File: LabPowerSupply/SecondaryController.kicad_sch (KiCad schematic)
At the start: 18 parts, among them Y2 8M

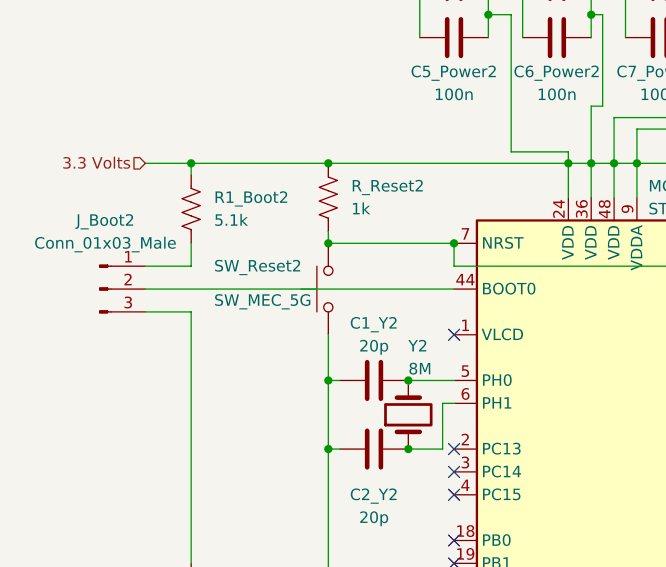
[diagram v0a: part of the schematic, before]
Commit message: Figured out how to make fill zones
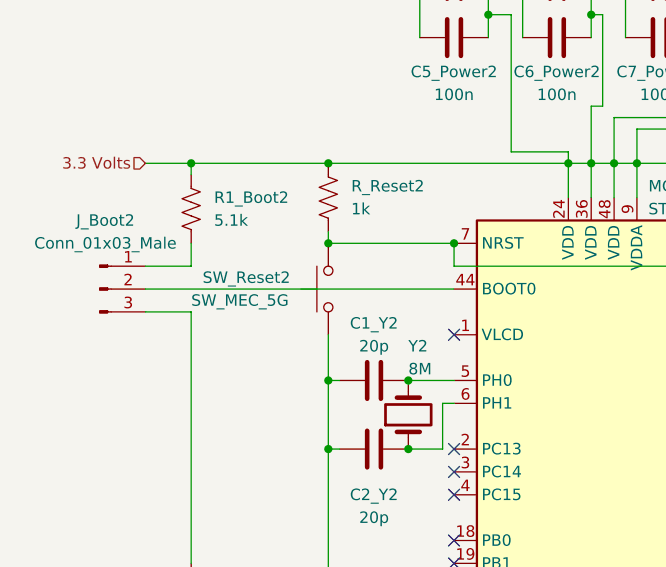
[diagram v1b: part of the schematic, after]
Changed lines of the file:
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@@
   (junction (at 116.84 139.7) (diameter 0) (color 0 0 0 0)
   )
+  (junction (at 68.58 63.5) (diameter 0) (color 0 0 0 0)
+  )
   (junction (at 68.58 54.61) (diameter 0) (color 0 0 0 0)
   )
@@
   (junction (at 101.6 30.48) (diameter 0) (color 0 0 0 0)
   )
-  (junction (at 68.58 63.5) (diameter 0) (color 0 0 0 0)
+  (junction (at 82.55 63.5) (diameter 0) (color 0 0 0 0)
   )
   (junction (at 68.58 139.7) (diameter 0) (color 0 0 0 0)
@@
   )
   (junction (at 86.36 38.1) (diameter 0) (color 0 0 0 0)
-  )
-  (junction (at 82.55 63.5) (diameter 0) (color 0 0 0 0)
   )
   (junction (at 77.47 78.74) (diameter 0) (color 0 0 0 0)
@@
     (stroke (width 0) (type default) (color 0 0 0 0))
   )
+  (wire (pts (xy 100.33 54.61) (xy 102.87 54.61))
+    (stroke (width 0) (type default) (color 0 0 0 0))
+  )
+  (wire (pts (xy 106.68 138.43) (xy 106.68 66.04))
+    (stroke (width 0) (type default) (color 0 0 0 0))
+  )
+  (wire (pts (xy 48.26 66.04) (xy 53.34 66.04))
+    (stroke (width 0) (type default) (color 0 0 0 0))
+  )
+  (wire (pts (xy 102.87 50.8) (xy 102.87 54.61))
+    (stroke (width 0) (type default) (color 0 0 0 0))
+  )
   (wire (pts (xy 68.58 63.5) (xy 82.55 63.5))
-    (stroke (width 0) (type default) (color 0 0 0 0))
-  )
-  (wire (pts (xy 100.33 54.61) (xy 102.87 54.61))
-    (stroke (width 0) (type default) (color 0 0 0 0))
-  )
-  (wire (pts (xy 106.68 138.43) (xy 106.68 66.04))
-    (stroke (width 0) (type default) (color 0 0 0 0))
-  )
-  (wire (pts (xy 48.26 66.04) (xy 53.34 66.04))
-    (stroke (width 0) (type default) (color 0 0 0 0))
-  )
-  (wire (pts (xy 102.87 50.8) (xy 102.87 54.61))
     (stroke (width 0) (type default) (color 0 0 0 0))
   )
@@
     (pin "2")
   )
+  (symbol (lib_id "Switch:SW_MEC_5G") (at 68.58 68.58 90) (unit 1)
+    (in_bom yes) (on_board yes)
+    (property "Reference" "SW_Reset2" (id 0) (at 54.61 67.31 90)
+      (effects (font (size 1.27 1.27)) (justify right))
+    )
+    (property "Value" "SW_MEC_5G" (id 1) (at 53.34 69.85 90)
+      (effects (font (size 1.27 1.27)) (justify right))
+    )
+    (property "Footprint" "Button_Switch_THT:SW_PUSH-12mm" (id 2) (at 63.5 68.58 0)
+      (effects (font (size 1.27 1.27)) hide)
+    )
+    (property "Datasheet" "http://www.apem.com/int/index.php?controller=attachment&id_attachment=488" (id 3) (at 63.5 68.58 0)
+      (effects (font (size 1.27 1.27)) hide)
+    )
+    (pin "1")
+    (pin "3")
+    (pin "2")
+    (pin "4")
+  )
   (symbol (lib_id "Device:C") (at 105.41 34.29 90) (unit 1)
     (in_bom yes) (on_board yes) (fields_autoplaced)
@@
     (pin "2")
   )
-  (symbol (lib_id "Switch:SW_MEC_5G") (at 68.58 68.58 90) (unit 1)
-    (in_bom yes) (on_board yes)
-    (property "Reference" "SW_Reset2" (id 0) (at 55.88 66.04 90)
-      (effects (font (size 1.27 1.27)) (justify right))
-    )
-    (property "Value" "SW_MEC_5G" (id 1) (at 55.88 69.85 90)
-      (effects (font (size 1.27 1.27)) (justify right))
-    )
-    (property "Footprint" "Button_Switch_THT:SW_PUSH-12mm" (id 2) (at 63.5 68.58 0)
-      (effects (font (size 1.27 1.27)) hide)
-    )
-    (property "Datasheet" "http://www.apem.com/int/index.php?controller=attachment&id_attachment=488" (id 3) (at 63.5 68.58 0)
-      (effects (font (size 1.27 1.27)) hide)
-    )
-    (pin "1")
-    (pin "3")
-    (pin "2")
-    (pin "4")
-  )
 )

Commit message: Traces
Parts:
- SW_Reset2: symbol Switch:SW_MEC_5G -> Switch:SW_Push
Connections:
- net GND: no longer SW_Reset2.2 (A)
- net at J_STLink2.5 (Pin_5), MCU_2.7 (NRST), R_Reset2.2: now also SW_Reset2.2; no longer SW_Reset2.3 (B), SW_Reset2.4 (B)
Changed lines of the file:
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@@
     (pin "2")
   )
-  (symbol (lib_id "Switch:SW_MEC_5G") (at 68.58 68.58 90) (unit 1)
+  (symbol (lib_id "Switch:SW_Push") (at 68.58 68.58 90) (unit 1)
     (in_bom yes) (on_board yes)
     (property "Reference" "SW_Reset2" (id 0) (at 54.61 67.31 90)
@@
       (effects (font (size 1.27 1.27)) hide)
     )
-    (property "Datasheet" "http://www.apem.com/int/index.php?controller=attachment&id_attachment=488" (id 3) (at 63.5 68.58 0)
+    (property "Datasheet" "~" (id 3) (at 63.5 68.58 0)
       (effects (font (size 1.27 1.27)) hide)
     )
     (pin "1")
-    (pin "3")
     (pin "2")
-    (pin "4")
   )
   (symbol (lib_id "Device:C") (at 105.41 34.29 90) (unit 1)

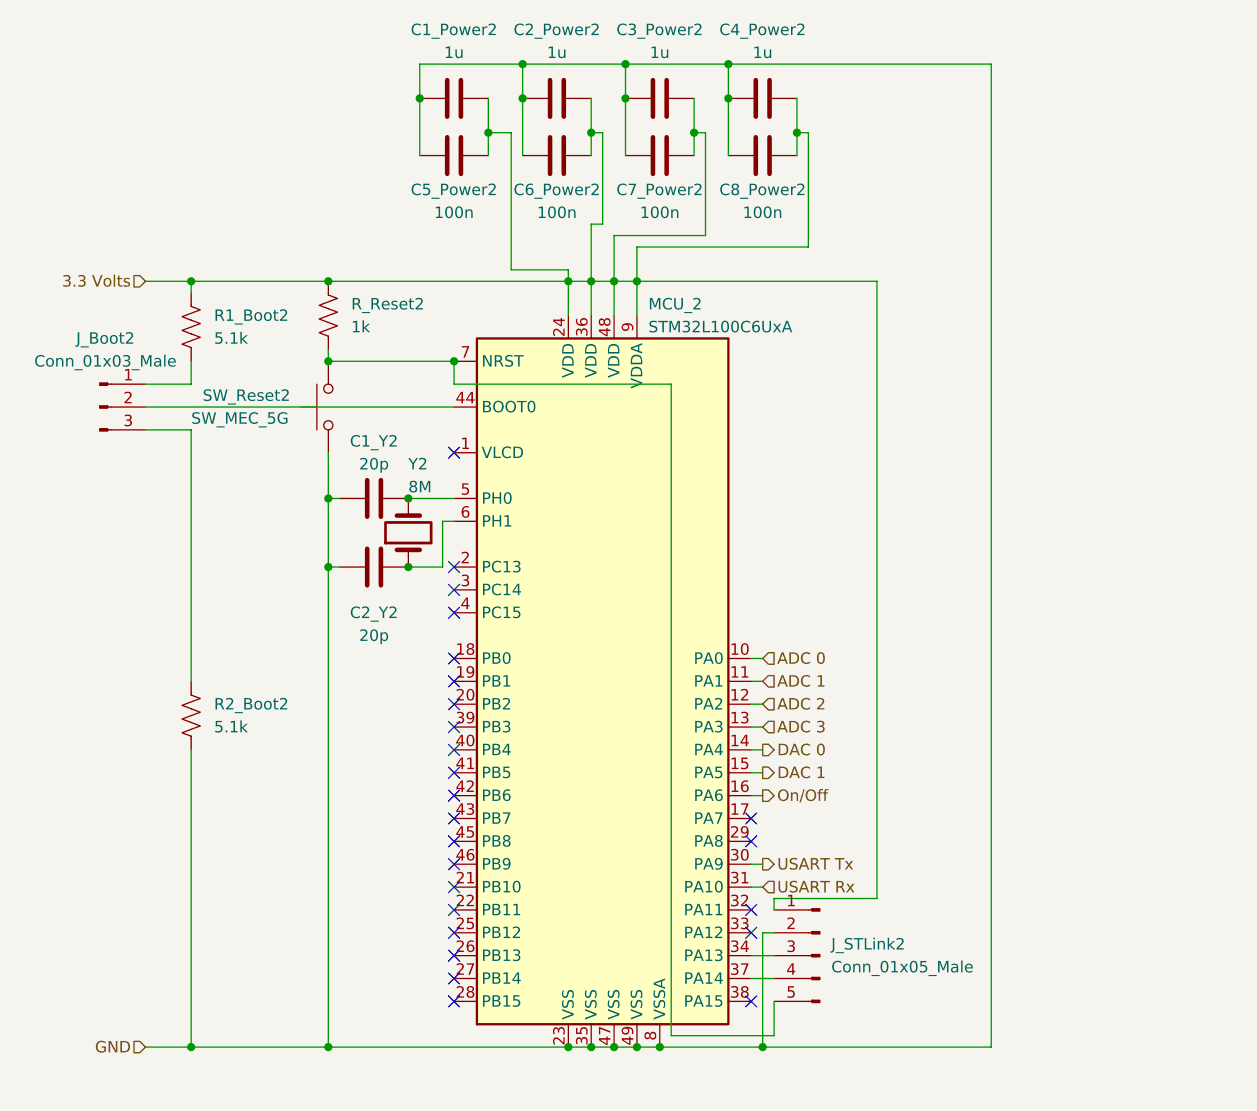
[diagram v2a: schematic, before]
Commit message: Started ch2 MCU routing
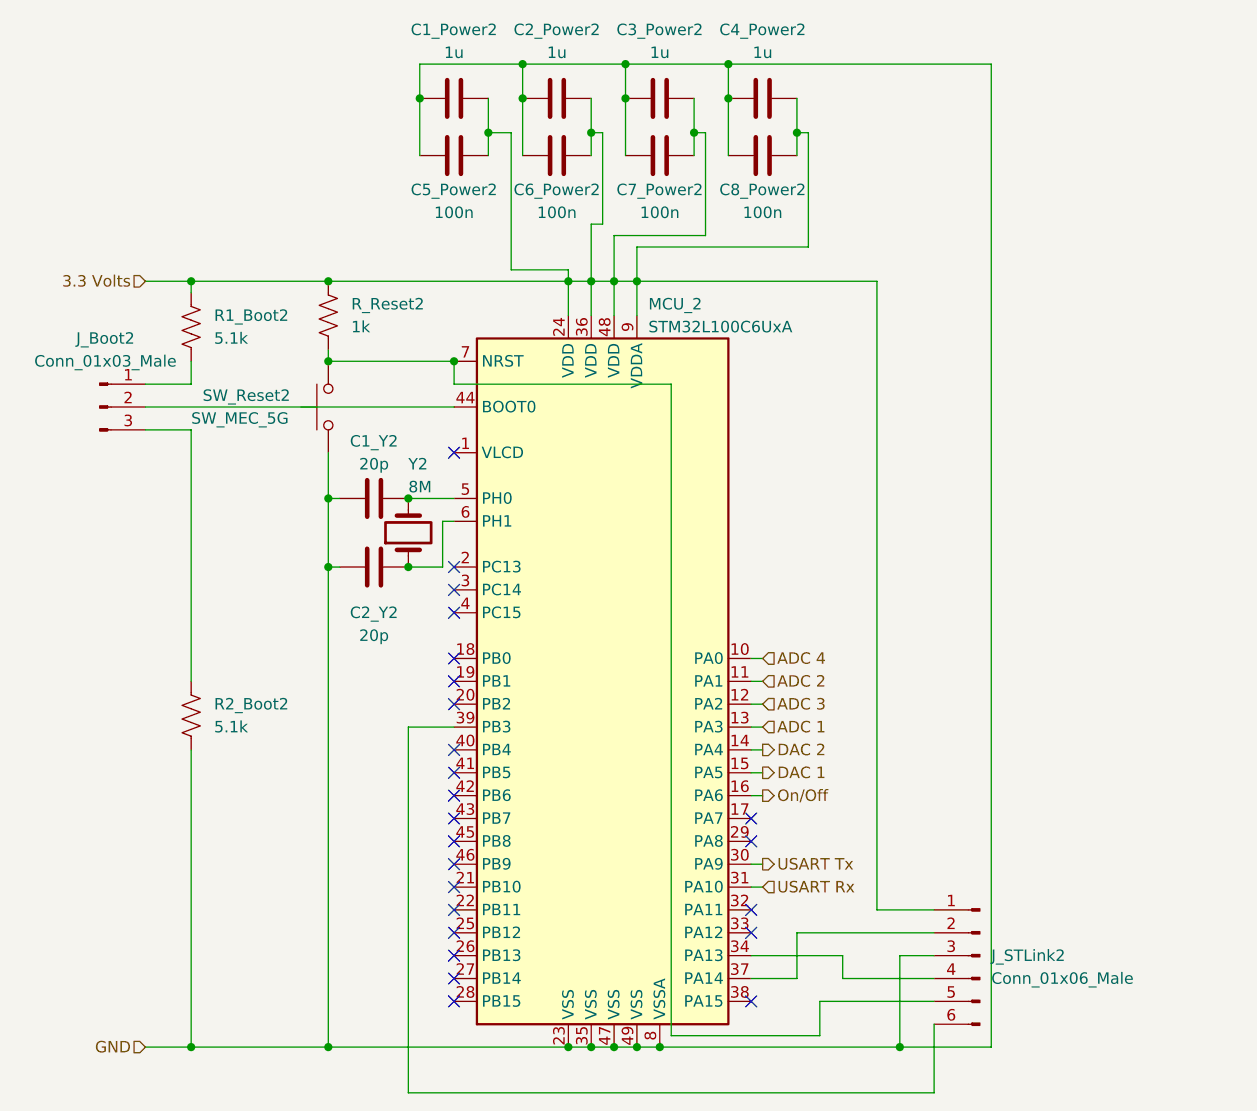
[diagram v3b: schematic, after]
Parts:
- removed J_STLink2: Conn_01x05_Male, Connector_PinHeader_2.54mm:PinHeader_1x05_P2.54mm_Vertical, symbol Connector:Conn_01x05_Male
- added J_STLink2: Conn_01x06_Male, Connector_PinHeader_2.54mm:PinHeader_1x06_P2.54mm_Vertical, symbol Connector:Conn_01x06_Male
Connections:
- net 3.3 Volts: now also J_STLink2.1 (Pin_1)
- net ADC 1: now also MCU_2.13 (PA3); no longer MCU_2.11 (PA1)
- net ADC 2: now also MCU_2.11 (PA1); no longer MCU_2.12 (PA2)
- net ADC 3: now also MCU_2.12 (PA2); no longer MCU_2.13 (PA3)
- net GND: now also J_STLink2.3 (Pin_3)
- net at MCU_2.34 (PA13): now also J_STLink2.4 (Pin_4)
- net at MCU_2.37 (PA14): now also J_STLink2.2 (Pin_2)
- net at MCU_2.7 (NRST), R_Reset2.2, SW_Reset2.2: now also J_STLink2.5 (Pin_5)
- net at MCU_2.39 (PB3): now also J_STLink2.6 (Pin_6)
- net ADC 0 renamed ADC 4
- net DAC 0 renamed DAC 2
- no-connect marks 25 -> 24
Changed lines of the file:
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@@
   (junction (at 102.87 139.7) (diameter 0) (color 0 0 0 0)
   )
-  (junction (at 116.84 139.7) (diameter 0) (color 0 0 0 0)
-  )
   (junction (at 68.58 63.5) (diameter 0) (color 0 0 0 0)
   )
@@
   )
   (junction (at 97.79 139.7) (diameter 0) (color 0 0 0 0)
+  )
+  (junction (at 132.08 139.7) (diameter 0) (color 0 0 0 0)
   )
   (junction (at 109.22 38.1) (diameter 0) (color 0 0 0 0)
@@
   (no_connect (at 82.55 109.22))
   (no_connect (at 82.55 106.68))
-  (no_connect (at 82.55 104.14))
   (no_connect (at 82.55 121.92))
   (no_connect (at 82.55 119.38))
@@
     (stroke (width 0) (type default) (color 0 0 0 0))
   )
+  (wire (pts (xy 82.55 104.14) (xy 77.47 104.14))
+    (stroke (width 0) (type default) (color 0 0 0 0))
+  )
   (wire (pts (xy 48.26 71.12) (xy 53.34 71.12))
     (stroke (width 0) (type default) (color 0 0 0 0))
@@
     (stroke (width 0) (type default) (color 0 0 0 0))
   )
-  (wire (pts (xy 118.11 123.19) (xy 129.54 123.19))
-    (stroke (width 0) (type default) (color 0 0 0 0))
-  )
   (wire (pts (xy 97.79 34.29) (xy 97.79 38.1))
     (stroke (width 0) (type default) (color 0 0 0 0))
   )
+  (wire (pts (xy 120.65 127) (xy 135.89 127))
+    (stroke (width 0) (type default) (color 0 0 0 0))
+  )
   (wire (pts (xy 86.36 38.1) (xy 88.9 38.1))
     (stroke (width 0) (type default) (color 0 0 0 0))
   )
+  (wire (pts (xy 129.54 124.46) (xy 135.89 124.46))
+    (stroke (width 0) (type default) (color 0 0 0 0))
+  )
   (wire (pts (xy 100.33 54.61) (xy 102.87 54.61))
     (stroke (width 0) (type default) (color 0 0 0 0))
@@
     (stroke (width 0) (type default) (color 0 0 0 0))
   )
-  (wire (pts (xy 118.11 127) (xy 116.84 127))
-    (stroke (width 0) (type default) (color 0 0 0 0))
-  )
   (wire (pts (xy 115.57 121.92) (xy 116.84 121.92))
     (stroke (width 0) (type default) (color 0 0 0 0))
   )
+  (wire (pts (xy 125.73 129.54) (xy 125.73 132.08))
+    (stroke (width 0) (type default) (color 0 0 0 0))
+  )
+  (wire (pts (xy 132.08 139.7) (xy 142.24 139.7))
+    (stroke (width 0) (type default) (color 0 0 0 0))
+  )
+  (wire (pts (xy 77.47 104.14) (xy 77.47 144.78))
+    (stroke (width 0) (type default) (color 0 0 0 0))
+  )
   (wire (pts (xy 88.9 53.34) (xy 95.25 53.34))
     (stroke (width 0) (type default) (color 0 0 0 0))
   )
-  (wire (pts (xy 118.11 124.46) (xy 118.11 123.19))
+  (wire (pts (xy 132.08 129.54) (xy 132.08 139.7))
     (stroke (width 0) (type default) (color 0 0 0 0))
   )
@@
     (stroke (width 0) (type default) (color 0 0 0 0))
   )
-  (wire (pts (xy 115.57 129.54) (xy 118.11 129.54))
+  (wire (pts (xy 115.57 129.54) (xy 125.73 129.54))
     (stroke (width 0) (type default) (color 0 0 0 0))
   )
@@
     (stroke (width 0) (type default) (color 0 0 0 0))
   )
-  (wire (pts (xy 118.11 134.62) (xy 118.11 138.43))
+  (wire (pts (xy 123.19 134.62) (xy 123.19 138.43))
     (stroke (width 0) (type default) (color 0 0 0 0))
   )
@@
     (stroke (width 0) (type default) (color 0 0 0 0))
   )
-  (wire (pts (xy 129.54 123.19) (xy 129.54 54.61))
+  (wire (pts (xy 129.54 54.61) (xy 129.54 124.46))
     (stroke (width 0) (type default) (color 0 0 0 0))
   )
@@
     (stroke (width 0) (type default) (color 0 0 0 0))
   )
+  (wire (pts (xy 77.47 144.78) (xy 135.89 144.78))
+    (stroke (width 0) (type default) (color 0 0 0 0))
+  )
   (wire (pts (xy 97.79 54.61) (xy 97.79 58.42))
     (stroke (width 0) (type default) (color 0 0 0 0))
@@
     (stroke (width 0) (type default) (color 0 0 0 0))
   )
-  (wire (pts (xy 116.84 127) (xy 116.84 139.7))
-    (stroke (width 0) (type default) (color 0 0 0 0))
-  )
   (wire (pts (xy 81.28 86.36) (xy 77.47 86.36))
     (stroke (width 0) (type default) (color 0 0 0 0))
@@
     (stroke (width 0) (type default) (color 0 0 0 0))
   )
-  (wire (pts (xy 115.57 132.08) (xy 118.11 132.08))
+  (wire (pts (xy 115.57 132.08) (xy 120.65 132.08))
     (stroke (width 0) (type default) (color 0 0 0 0))
   )
@@
     (stroke (width 0) (type default) (color 0 0 0 0))
   )
-  (wire (pts (xy 105.41 139.7) (xy 116.84 139.7))
-    (stroke (width 0) (type default) (color 0 0 0 0))
-  )
   (wire (pts (xy 115.57 96.52) (xy 116.84 96.52))
     (stroke (width 0) (type default) (color 0 0 0 0))
@@
     (stroke (width 0) (type default) (color 0 0 0 0))
   )
+  (wire (pts (xy 120.65 132.08) (xy 120.65 127))
+    (stroke (width 0) (type default) (color 0 0 0 0))
+  )
   (wire (pts (xy 100.33 49.53) (xy 100.33 54.61))
     (stroke (width 0) (type default) (color 0 0 0 0))
@@
     (stroke (width 0) (type default) (color 0 0 0 0))
   )
-  (wire (pts (xy 116.84 139.7) (xy 142.24 139.7))
-    (stroke (width 0) (type default) (color 0 0 0 0))
-  )
   (wire (pts (xy 110.49 38.1) (xy 110.49 49.53))
     (stroke (width 0) (type default) (color 0 0 0 0))
@@
     (stroke (width 0) (type default) (color 0 0 0 0))
   )
-  (wire (pts (xy 118.11 138.43) (xy 106.68 138.43))
+  (wire (pts (xy 123.19 138.43) (xy 106.68 138.43))
     (stroke (width 0) (type default) (color 0 0 0 0))
   )
@@
     (stroke (width 0) (type default) (color 0 0 0 0))
   )
+  (wire (pts (xy 105.41 139.7) (xy 132.08 139.7))
+    (stroke (width 0) (type default) (color 0 0 0 0))
+  )
+  (wire (pts (xy 135.89 144.78) (xy 135.89 137.16))
+    (stroke (width 0) (type default) (color 0 0 0 0))
+  )
+  (wire (pts (xy 123.19 134.62) (xy 135.89 134.62))
+    (stroke (width 0) (type default) (color 0 0 0 0))
+  )
   (wire (pts (xy 101.6 34.29) (xy 101.6 40.64))
     (stroke (width 0) (type default) (color 0 0 0 0))
   )
+  (wire (pts (xy 125.73 132.08) (xy 135.89 132.08))
+    (stroke (width 0) (type default) (color 0 0 0 0))
+  )
   (wire (pts (xy 115.57 104.14) (xy 116.84 104.14))
     (stroke (width 0) (type default) (color 0 0 0 0))
@@
     (stroke (width 0) (type default) (color 0 0 0 0))
   )
-  (hierarchical_label "ADC 3" (shape input) (at 116.84 104.14 0)
+  (wire (pts (xy 135.89 129.54) (xy 132.08 129.54))
+    (stroke (width 0) (type default) (color 0 0 0 0))
+  )
+  (hierarchical_label "ADC 1" (shape input) (at 116.84 104.14 0)
     (effects (font (size 1.27 1.27)) (justify left))
   )
@@
     (effects (font (size 1.27 1.27)) (justify left))
   )
-  (hierarchical_label "ADC 0" (shape input) (at 116.84 96.52 0)
-    (effects (font (size 1.27 1.27)) (justify left))
-  )
-  (hierarchical_label "ADC 1" (shape input) (at 116.84 99.06 0)
-    (effects (font (size 1.27 1.27)) (justify left))
-  )
-  (hierarchical_label "ADC 2" (shape input) (at 116.84 101.6 0)
+  (hierarchical_label "ADC 4" (shape input) (at 116.84 96.52 0)
+    (effects (font (size 1.27 1.27)) (justify left))
+  )
+  (hierarchical_label "ADC 2" (shape input) (at 116.84 99.06 0)
+    (effects (font (size 1.27 1.27)) (justify left))
+  )
+  (hierarchical_label "ADC 3" (shape input) (at 116.84 101.6 0)
     (effects (font (size 1.27 1.27)) (justify left))
   )
@@
     (effects (font (size 1.27 1.27)) (justify left))
   )
-  (hierarchical_label "DAC 0" (shape output) (at 116.84 106.68 0)
+  (hierarchical_label "DAC 2" (shape output) (at 116.84 106.68 0)
     (effects (font (size 1.27 1.27)) (justify left))
   )
@@
     (pin "2")
   )
+  (symbol (lib_id "Connector:Conn_01x06_Male") (at 140.97 129.54 0) (mirror y) (unit 1)
+    (in_bom yes) (on_board yes) (fields_autoplaced)
+    (property "Reference" "J_STLink2" (id 0) (at 142.24 129.5399 0)
+      (effects (font (size 1.27 1.27)) (justify right))
+    )
+    (property "Value" "Conn_01x06_Male" (id 1) (at 142.24 132.0799 0)
+      (effects (font (size 1.27 1.27)) (justify right))
+    )
+    (property "Footprint" "Connector_PinHeader_2.54mm:PinHeader_1x06_P2.54mm_Vertical" (id 2) (at 140.97 129.54 0)
+      (effects (font (size 1.27 1.27)) hide)
+    )
+    (property "Datasheet" "~" (id 3) (at 140.97 129.54 0)
+      (effects (font (size 1.27 1.27)) hide)
+    )
+    (pin "1")
+    (pin "2")
+    (pin "3")
+    (pin "4")
+    (pin "5")
+    (pin "6")
+  )
   (symbol (lib_id "Device:C") (at 73.66 86.36 90) (mirror x) (unit 1)
     (in_bom yes) (on_board yes)
@@
     (pin "3")
   )
-  (symbol (lib_id "Connector:Conn_01x05_Male") (at 123.19 129.54 0) (mirror y) (unit 1)
-    (in_bom yes) (on_board yes) (fields_autoplaced)
-    (property "Reference" "J_STLink2" (id 0) (at 124.46 128.2699 0)
-      (effects (font (size 1.27 1.27)) (justify right))
-    )
-    (property "Value" "Conn_01x05_Male" (id 1) (at 124.46 130.8099 0)
-      (effects (font (size 1.27 1.27)) (justify right))
-    )
-    (property "Footprint" "Connector_PinHeader_2.54mm:PinHeader_1x05_P2.54mm_Vertical" (id 2) (at 123.19 129.54 0)
-      (effects (font (size 1.27 1.27)) hide)
-    )
-    (property "Datasheet" "~" (id 3) (at 123.19 129.54 0)
-      (effects (font (size 1.27 1.27)) hide)
-    )
-    (pin "1")
-    (pin "2")
-    (pin "3")
-    (pin "4")
-    (pin "5")
-  )
   (symbol (lib_id "MCU_ST_STM32L1:STM32L100C6UxA") (at 100.33 99.06 0) (unit 1)

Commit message: Nearly finished
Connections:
- net ADC 2: now also MCU_2.10 (PA0); no longer MCU_2.11 (PA1)
- net ADC 4: now also MCU_2.11 (PA1); no longer MCU_2.10 (PA0)
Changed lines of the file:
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@@
     (effects (font (size 1.27 1.27)) (justify left))
   )
-  (hierarchical_label "ADC 4" (shape input) (at 116.84 96.52 0)
+  (hierarchical_label "ADC 2" (shape input) (at 116.84 96.52 0)
     (effects (font (size 1.27 1.27)) (justify left))
   )
-  (hierarchical_label "ADC 2" (shape input) (at 116.84 99.06 0)
+  (hierarchical_label "ADC 4" (shape input) (at 116.84 99.06 0)
     (effects (font (size 1.27 1.27)) (justify left))
   )

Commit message: Rev 1.0 done
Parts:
- added A1_2, D2_2: Conn_01x01_Male, symbol Connector:Conn_01x01_Male
- added ADC342_2: Conn_01x03_Male, Connector_PinHeader_2.54mm:PinHeader_1x03_P2.54mm_Vertical, symbol Connector:Conn_01x03_Male
- added D1_2: (no value), symbol Connector:Conn_01x01_Male
- J_Boot2: footprint Connector_PinSocket_2.54mm:PinSocket_1x03_P2.54mm_Vertical -> (none)
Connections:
- net ADC 1: now also A1_2.1 (Pin_1)
- net ADC 2: now also ADC342_2.1 (Pin_1)
- net ADC 3: now also ADC342_2.3 (Pin_3)
- net ADC 4: now also ADC342_2.2 (Pin_2)
- net DAC 1: now also D1_2.1 (Pin_1)
- net DAC 2: now also D2_2.1 (Pin_1)
